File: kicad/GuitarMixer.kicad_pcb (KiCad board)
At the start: 2 copper layers, 73.8 x 56.6 mm, 50 parts, among them J1 Conn_01x03_Pin, J2 Conn_01x03_Pin, J3 Conn_01x03_Pin, J4 Conn_01x02_Pin, J5 Conn_01x02_Pin, J6 Conn_01x03_Pin, Q1 2N5457, SW1 SW_SPST, U1 TL072, U2 TL072

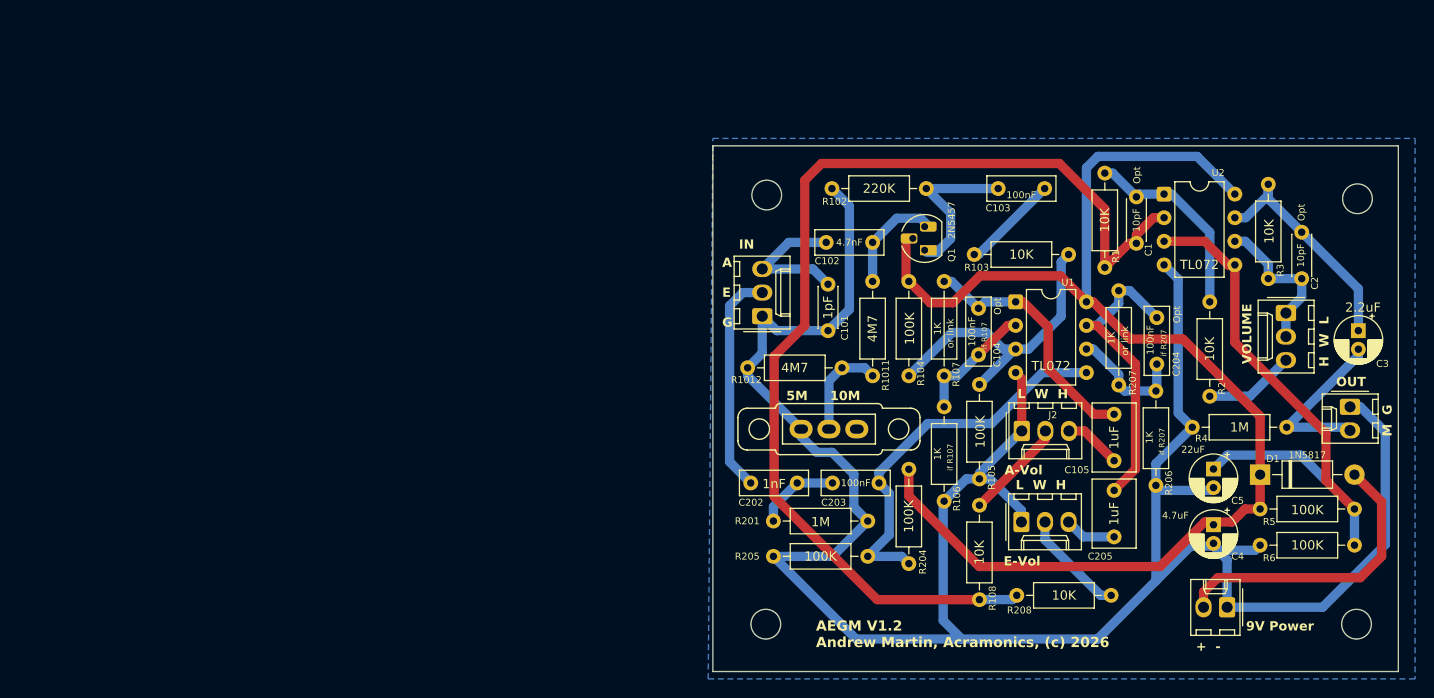
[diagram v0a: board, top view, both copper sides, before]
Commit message: New version with split rail power supply
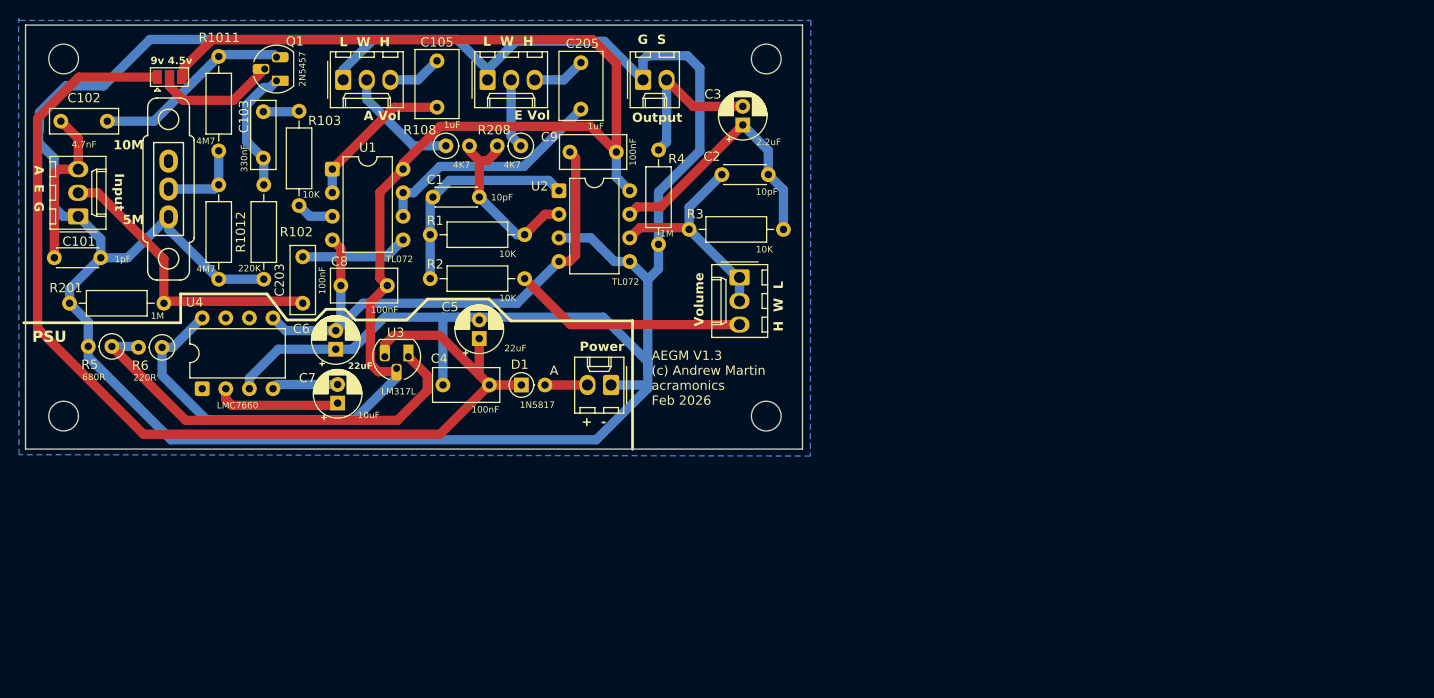
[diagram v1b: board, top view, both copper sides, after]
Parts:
- removed C104, C204: 100nF, Capacitor_THT:C_Rect_L7.2mm_W2.5mm_P5.00mm_FKS2_FKP2_MKS2_MKP2
- removed C202: 1nF, Capacitor_THT:C_Rect_L7.2mm_W2.5mm_P5.00mm_FKS2_FKP2_MKS2_MKP2
- removed R104, R105, R204, R205: 100K, Resistor_THT:R_Axial_DIN0207_L6.3mm_D2.5mm_P10.16mm_Horizontal
- removed R106, R107, R206, R207: 1K, Resistor_THT:R_Axial_DIN0207_L6.3mm_D2.5mm_P10.16mm_Horizontal
- removed the REF** at (107.8, 59.7)
- removed the REF** at (171.3, 105.9)
- removed the REF** at (171.4, 60.1)
- removed the REF** at (107.7, 105.9)
- added C6: 22uF, Capacitor_THT:CP_Radial_D5.0mm_P2.00mm, F.Cu at (61.4, 76.3)
- added C7: 10uF, Capacitor_THT:CP_Radial_D5.0mm_P2.00mm, F.Cu at (61.6, 82.1)
- added C8: 100nF, Capacitor_THT:C_Rect_L7.0mm_W3.5mm_P5.00mm, F.Cu at (67.0, 69.5)
- added C9: 100nF, Capacitor_THT:C_Rect_L7.0mm_W3.5mm_P5.00mm, F.Cu at (91.6, 55.1)
- added JP1: Jumper_3_Open, Jumper:SolderJumper-3_P1.3mm_Open_Pad1.0x1.5mm, F.Cu at (43.5, 47.0)
- added REF**: MountingHole_3.2mm_M3, MountingHole:MountingHole_3.2mm_M3, F.Cu at (32.1, 83.5)
- added REF**: MountingHole_3.2mm_M3, MountingHole:MountingHole_3.2mm_M3, F.Cu at (107.8, 45.0)
- added REF**: MountingHole_3.2mm_M3, MountingHole:MountingHole_3.2mm_M3, F.Cu at (32.1, 45.0)
- added REF**: MountingHole_3.2mm_M3, MountingHole:MountingHole_3.2mm_M3, F.Cu at (107.8, 83.5)
- added U3: LM317L, Package_TO_SOT_THT:TO-92_HandSolder, F.Cu at (69.2, 77.1)
- added U4: LMC7660, Package_DIP:DIP-8_W7.62mm, F.Cu at (47.0, 80.5)
- C103: value 100nF -> 330nF
- C4: value 4.7uF -> 100nF; footprint Capacitor_THT:CP_Radial_D5.0mm_P2.00mm -> Capacitor_THT:C_Rect_L7.0mm_W3.5mm_P5.00mm
- D1: footprint Diode_THT:D_DO-41_SOD81_P10.16mm_Horizontal -> Diode_THT:D_DO-35_SOD27_P2.54mm_Vertical_AnodeUp
- R108, R208: value 10K -> 4K7; footprint Resistor_THT:R_Axial_DIN0207_L6.3mm_D2.5mm_P10.16mm_Horizontal -> Resistor_THT:R_Axial_DIN0207_L6.3mm_D2.5mm_P2.54mm_Vertical
- R5: value 100K -> 680R; footprint Resistor_THT:R_Axial_DIN0207_L6.3mm_D2.5mm_P10.16mm_Horizontal -> Resistor_THT:R_Axial_DIN0207_L6.3mm_D2.5mm_P2.54mm_Vertical
- R6: value 100K -> 220R; footprint Resistor_THT:R_Axial_DIN0207_L6.3mm_D2.5mm_P10.16mm_Horizontal -> Resistor_THT:R_Axial_DIN0207_L6.3mm_D2.5mm_P2.54mm_Vertical
- moved R5 134.9 mm to (37.3, 76.0)
- moved R6 120.1 mm to (42.7, 76.1), turned to 180 degrees
- moved J5 83.9 mm to (94.5, 47.3), turned to 0 degrees
- moved C102 83.4 mm to (31.8, 51.8)
- moved C101 83.3 mm to (31.1, 66.5), turned to 0 degrees
- moved J2 82.3 mm to (62.2, 47.3)
- moved C5 80.3 mm to (76.8, 75.2), turned to 90 degrees
- moved D1 80.1 mm to (81.4, 80.2)
- moved C105 80.0 mm to (72.3, 50.2), turned to 90 degrees
- moved R208 79.9 mm to (81.3, 54.4)
- moved C4 79.4 mm to (77.9, 80.2), turned to 180 degrees
- moved C103 79.2 mm to (53.6, 55.7), turned to 90 degrees
- moved SW1 75.7 mm to (43.4, 59.0), turned to 90 degrees
- moved U1 74.9 mm to (61.0, 56.9)
- moved R2 74.8 mm to (81.7, 68.7), turned to 180 degrees
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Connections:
- net +9V renamed Net-(D1-A)
- C105 pad 1: Net-(C104-Pad2) -> Net-(U1A--)
- C203 pad 1: Net-(C202-Pad2) -> Net-(J1-Pin_2)
- C205 pad 1: Net-(C204-Pad2) -> Net-(U1B--)
- C5 pad 1: +4V -> +9VA
- Q1 pad 2: +9VA -> Net-(JP1-C)
- R201 pad 1: Net-(C202-Pad2) -> Net-(J1-Pin_2)
- R5 pad 1: +4V -> Net-(U3-ADJ)
- R5 pad 2: +9VA -> Earth
- R6 pad 1: Earth -> +4.5V
- R6 pad 2: +4V -> Net-(U3-ADJ)
- U1 pad 1: Net-(C104-Pad2) -> Net-(U1A--)
- U1 pad 4: Earth -> -4.5V
- U1 pad 7: Net-(C204-Pad2) -> Net-(U1B--)
- U1 pad 8: +9VA -> +4.5V
- U2 pad 3: +4V -> Earth
- U2 pad 4: Earth -> -4.5V
- U2 pad 5: +4V -> Earth
- U2 pad 8: +9VA -> +4.5V
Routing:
- net +4.5V: track 0.00 -> 155.7 mm
- net Net-(U2A--): track 116.8 -> 19.3 mm
- net Earth: track 253.8 -> 319.3 mm
- net +4V: track 62.4 -> 0.00 mm
- net -4.5V: track 0.00 -> 58.0 mm
- net Net-(U3-ADJ): track 0.00 -> 46.0 mm
- net Net-(C204-Pad2): track 32.7 -> 0.00 mm
- net Net-(U1B-+): track 42.0 -> 11.6 mm
- net Net-(U1A-+): track 33.0 -> 4.06 mm
- net Net-(D1-A): track 32.4 -> 4.57 mm
- net Net-(C104-Pad2): track 27.4 -> 0.00 mm
- net +9VA: track 140.0 -> 115.3 mm
- net Net-(J6-Pin_3): track 9.81 -> 25.2 mm
- net Net-(U4-CAP+): track 0.00 -> 13.6 mm
- net Net-(JP1-C): track 0.00 -> 13.3 mm
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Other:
- board size 73.8 x 56.6 mm -> 83.7 x 45.6 mm
- board text added: "10M"
- board text added: "5M"
- board text added: "9v 4.5v"
- board text added: "A Vol"
- board text added: "AEGM V1.3 (c) Andrew Martin acramonics Feb 2026"
- board text added: "E Vol"
- board text added: "G S"
- board text added: "Input"
- board text added: "Output"
- board text added: "PSU"
- board text added: "Power"
- board text added: "Volume"
- board text removed: "5M 10M"
- board text removed: "9V Power"
- board text removed: "A-Vol"
- board text removed: "AEGM V1.2 Andrew Martin, Acramonics, (c) 2026"
- board text removed: "E-Vol"
- board text removed: "IN"
- board text removed: "M G"
- board text removed: "OUT"
- board text removed: "Opt"
- board text removed: "VOLUME"
- board text removed: "if R107"
- board text removed: "if R207"
- board text removed: "or link"
